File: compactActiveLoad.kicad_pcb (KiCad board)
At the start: 2 copper layers, 50 x 50 mm, 15 parts, among them CON1 Keystone_3002, CON2 Keystone_3002, CON3 LOAD, CON4 +12V, CON5 MOD, Q1 IRLR024NPBF, Q2 IRLR024NPBF, SW1 SW_1290F1123, SW2 SW_1290F1123, U1 Heatsink_55mm_CG128

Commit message: Placement
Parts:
- added C1: N.C., pnRLC:0603, F.Cu at (108.0, 138.5)
- added C2: 100n, 0603, F.Cu at (105.2, 135.2)
- added C3: 100n, 0805, F.Cu at (122.2, 111.5)
- added C4: 100n, 0805, F.Cu at (119.2, 107.8)
- added CON6: FAN, pnConnector:PAD2_2x3, F.Cu at (133.2, 103.8)
- added HS1: Heatsink_55mm_CG128, pnModules:Heatsink_55mm_CG128, B.Cu at (125.0, 125.0)
- added P1: 10k, pnRLC:pot_ACP_CA6VSMD+6001, F.Cu at (136.2, 146.2)
- added R1: 1k, pnRLC:0603, F.Cu at (124.2, 140.8)
- added R2: 100R, pnRLC:0603, F.Cu at (116.0, 136.2)
- added R3: 1R, pnRLC:R2010, F.Cu at (130.8, 132.2)
- added R4: 1R, pnRLC:R2010, F.Cu at (130.8, 128.8)
- added R5: 1R, pnRLC:R2010, F.Cu at (130.8, 135.8)
- added R6: 1R, pnRLC:R2010, F.Cu at (130.8, 139.2)
- added R7: 10k, pnRLC:0603, F.Cu at (105.2, 141.8)
- added R8: 1k, pnRLC:0603, F.Cu at (124.2, 143.0)
- added U2: LP2981A-50DBVR, pnSemiconductor:SOT23-5, F.Cu at (122.5, 107.8)
- U1: value Heatsink_55mm_CG128 -> LMV116MF; footprint pnModules:Heatsink_55mm_CG128 -> SOT23-5; moved to F.Cu
- moved REF** 68.3 mm to (56.8, 123.0)
- moved SW2 46.7 mm to (125.0, 148.0), turned to 0 degrees
- moved CON4 31.1 mm to (127.2, 110.2), turned to 180 degrees
- moved CON3 27.5 mm to (139.8, 137.5), turned to 90 degrees
- moved U1 24.6 mm to (104.4, 138.4), turned to 270 degrees
- moved CON5 16.5 mm to (114.5, 139.8)
- moved Q2 1.21 mm to (122.8, 130.5)
- moved SW1 1.00 mm to (118.0, 102.0)
- moved CON1 0.50 mm to (109.5, 117.0)
- moved CON2 0.50 mm to (140.5, 117.0)
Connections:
- CON1 pad +: Net-(CON1-Pad+) -> /Vbat
- CON2 pad +: Net-(CON2-Pad+) -> Net-(CON1-Pad-)
- CON2 pad -: Net-(CON2-Pad-) -> GND
- CON3 pad 1: Net-(CON3-Pad1) -> GND
- CON3 pad 2: Net-(CON3-Pad2) -> /Load
- CON4 pad 1: Net-(CON4-Pad1) -> GND
- CON4 pad 2: Net-(CON4-Pad2) -> /+12V
- CON5 pad 1: Net-(CON5-Pad1) -> GND
- Q1 pad 4: Net-(Q1-Pad4) -> /Load
- Q2 pad 1: Net-(Q2-Pad1) -> Net-(Q1-Pad1)
- Q2 pad 4: Net-(Q2-Pad4) -> /Load
- SW1 pad COM: Net-(SW1-PadCOM) -> VCC
- SW1 pad MNT: (no net) -> GND
- SW1 pad NC: Net-(SW1-PadNC) -> /Vbat
- SW1 pad NO: Net-(SW1-PadNO) -> /+5V
- SW2 pad COM: Net-(SW2-PadCOM) -> /Vin
- SW2 pad MNT: (no net) -> GND
- SW2 pad NO: Net-(SW2-PadNO) -> Net-(CON5-Pad2)
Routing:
- net (no net): track 0.00 -> 188.5 mm
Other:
- net class Default: clearance 0.2 -> 0.1524; trace_width 0.25 -> 0.1524; via_dia 0.6 -> 0.6048; via_drill 0.4 -> 0.3
- rule trace_clearance: 0.2 -> 0.1524
- rule trace_min: 0.2 -> 0.1524
- rule via_min_size: 0.4 -> 0.6048

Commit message: routing
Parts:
- removed REF** (x4): FIX-3-5, pnMechanical:FIX-3-5
- removed REF**: compactActiveLoad_BottomCover, pnMechanical:compactActiveLoad_BottomCover
- added C5: 10n, R0603, F.Cu at (114.5, 136.5)
- added MECH1: FIX-3-5, pnMechanical:FIX-3-5, F.Cu at (146.7, 146.7)
- added MECH2: FIX-3-5, pnMechanical:FIX-3-5, F.Cu at (146.7, 103.3)
- added MECH3: FIX-3-5, pnMechanical:FIX-3-5, F.Cu at (103.3, 103.3)
- added MECH4: FIX-3-5, pnMechanical:FIX-3-5, F.Cu at (103.3, 146.7)
- added MECH5: compactActiveLoad_BottomCover, pnMechanical:compactActiveLoad_BottomCover, F.Cu at (56.8, 123.0)
- added R9: 10k, R0603, F.Cu at (137.2, 141.0)
- C1, R1, R2, R7, R8: footprint pnRLC:0603 -> R0603
- C2: footprint 0603 -> R0603
- C3: value 100n -> 2u2u/25V; footprint 0805 -> R0805
- C4: value 100n -> TAJA106M010RNJ; footprint 0805 -> pnRLC:TANTAL_A
- P1: value 10k -> 1k
- moved R2 2.30 mm to (114.5, 134.5)
- moved C3 1.95 mm to (123.5, 110.0)
- moved U2 1.58 mm to (123.0, 106.2)
- moved CON6 1.27 mm to (134.5, 103.5), turned to 90 degrees
- moved R3 1.25 mm to (131.5, 133.2)
- moved R4 1.25 mm to (131.5, 129.8)
- moved R5 1.25 mm to (131.5, 136.8)
- moved R6 1.25 mm to (131.5, 140.2)
- moved CON4 0.75 mm to (128.0, 110.2)
- moved C4 0.56 mm to (119.8, 108.0), turned to 270 degrees
- turned R7 to 180 degrees
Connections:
- P1 pad 3: VCC -> Net-(P1-Pad3)
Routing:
- net (no net): track 188.5 -> 0.00 mm
- net VCC: track 0.00 -> 80.5 mm, vias 0 -> 6
- net Net-(CON1-Pad-): track 0.00 -> 53.4 mm, vias 0 -> 6
- net /Vbat: track 0.00 -> 39.8 mm, vias 0 -> 2
- net /Load: track 0.00 -> 29.1 mm, vias 0 -> 127
- net Net-(Q1-Pad3): track 0.00 -> 27.8 mm
- net /Vin: track 0.00 -> 27.0 mm
- net /+12V: track 0.00 -> 22.9 mm
- net Net-(Q1-Pad1): track 0.00 -> 21.6 mm
- net /Vfb: track 0.00 -> 21.3 mm
- net Net-(C5-Pad1): track 0.00 -> 19.8 mm, vias 0 -> 2
- net Net-(Q2-Pad3): track 0.00 -> 15.7 mm
- net GND: track 0.00 -> 15.2 mm, vias 0 -> 62
- net /Vout: track 0.00 -> 12.8 mm
- net Net-(P1-Pad2): track 0.00 -> 6.05 mm
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- added copper zone on F.Cu, net /Load
- added copper zone on F.Cu, net GND

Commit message: Routed
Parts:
- added TP1: GND, pnConnector:TP_1mm, F.Cu at (108.7, 144.1)
- added TP2: Vin, pnConnector:TP_1mm, F.Cu at (103.0, 140.5)
- added TP4: GND, pnConnector:TP_1mm, F.Cu at (102.5, 135.4)
- added TP5: Vout, pnConnector:TP_1mm, F.Cu at (108.3, 136.1)
- added TP6: Vfb, pnConnector:TP_1mm, F.Cu at (109.8, 140.3)
- added TP7: GND, pnConnector:TP_1mm, F.Cu at (142.4, 134.0)
- added TP8: Load, pnConnector:TP_1mm, F.Cu at (137.6, 136.2)
- SW1: value SW_1290F1123 -> Bat/Ext
- SW2: value SW_1290F1123 -> Ext/Int
- moved MECH5 3.11 mm to (55.2, 125.7)
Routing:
- net GND: track 15.2 -> 214.8 mm, vias 62 -> 84
- net /Load: track 29.1 -> 117.4 mm, vias 127 -> 135
- net Net-(CON1-Pad-): track 53.4 -> 84.0 mm, vias 6 -> 8
- net /Vout: track 12.8 -> 14.6 mm
- net /Vin: track 27.0 -> 28.2 mm
- net /Vfb: track 21.3 -> 22.3 mm
- net VCC: track 80.5 -> 81.4 mm
- net /Vbat: track 39.8 -> 39.4 mm, vias 2 -> 3
- added copper zone on B.Cu, net GND
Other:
- rule pad_to_mask_clearance: 0 -> 0.15
- board text added: "GND"

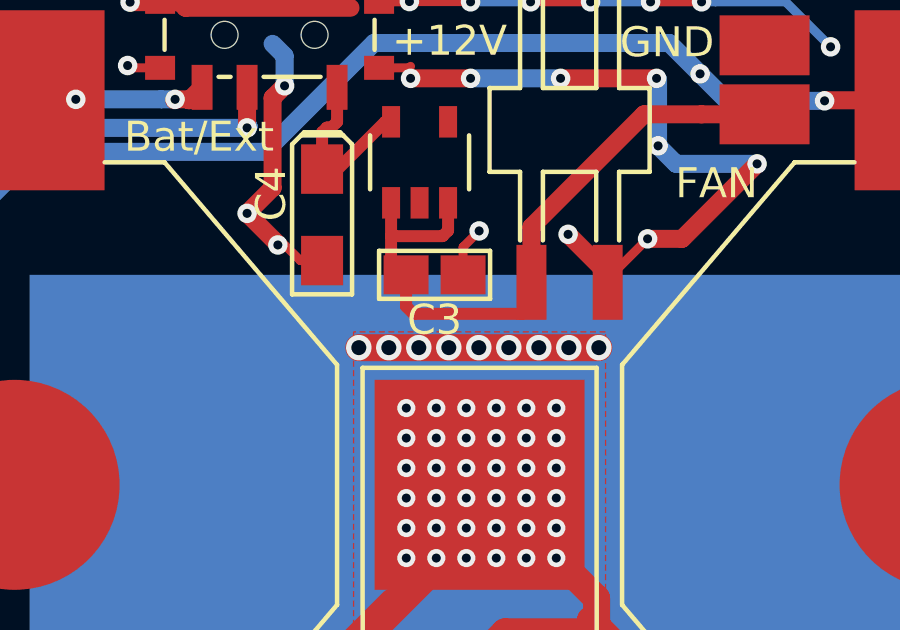
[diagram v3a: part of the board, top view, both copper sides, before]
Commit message: Little more thermal vias
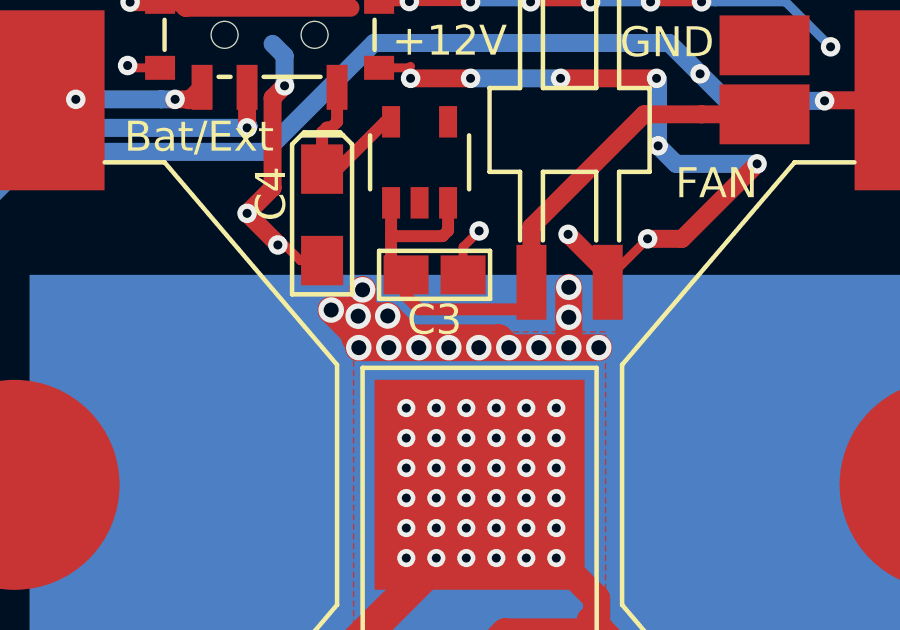
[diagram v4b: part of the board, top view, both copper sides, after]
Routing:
- net /Load: track 117.4 -> 134.9 mm, vias 135 -> 141
